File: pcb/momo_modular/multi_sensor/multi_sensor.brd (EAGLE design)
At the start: 100 x 33 mm, 38 parts, among them U1 MCP6001U, U10 SM5470-DIFF-PRESS-SENSOR, U2 16LF1847, U3 DUAL-BUFFER-OD-NC7WZ07, U4 LT1990, U5 2:1-MUX, U6 2:1-MUX, U7 AD8557-DIGITRIM-OPAMP, U8 2:1-MUX, U9 2:1-MUX

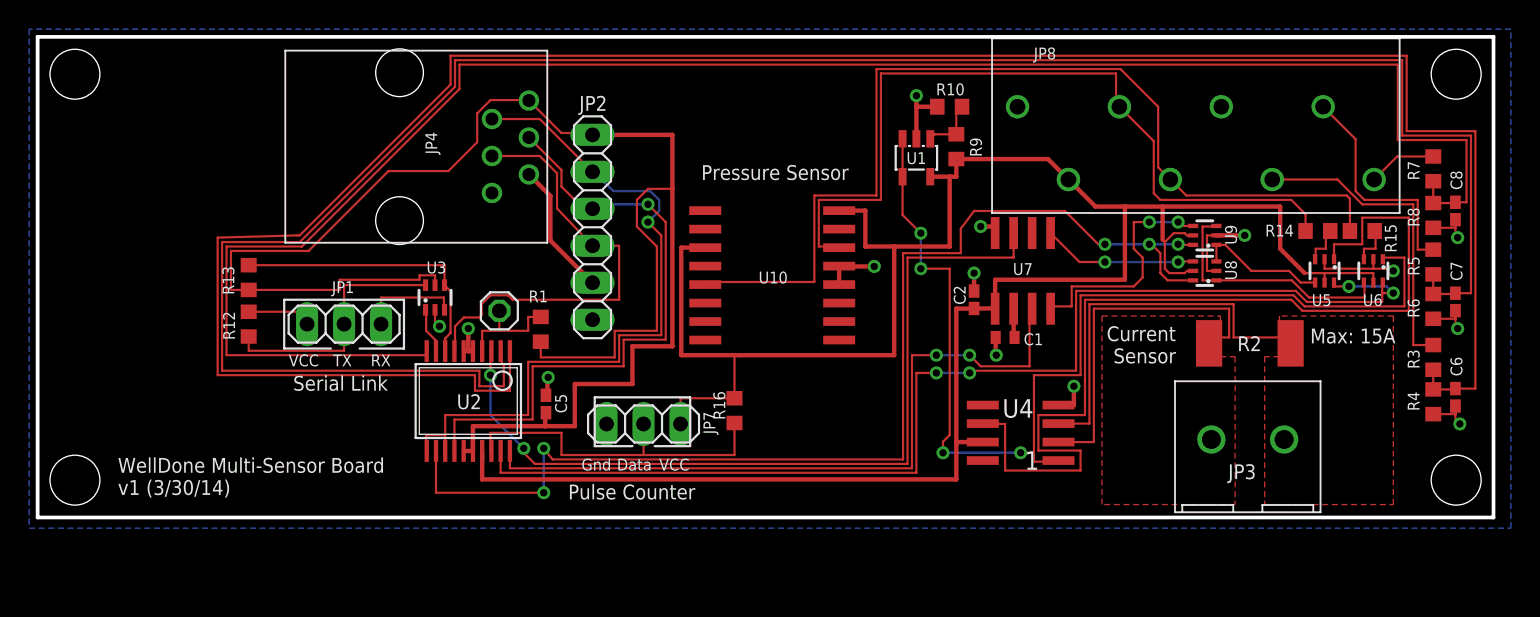
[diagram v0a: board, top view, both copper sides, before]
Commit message: Update BOM descriptions and footprints
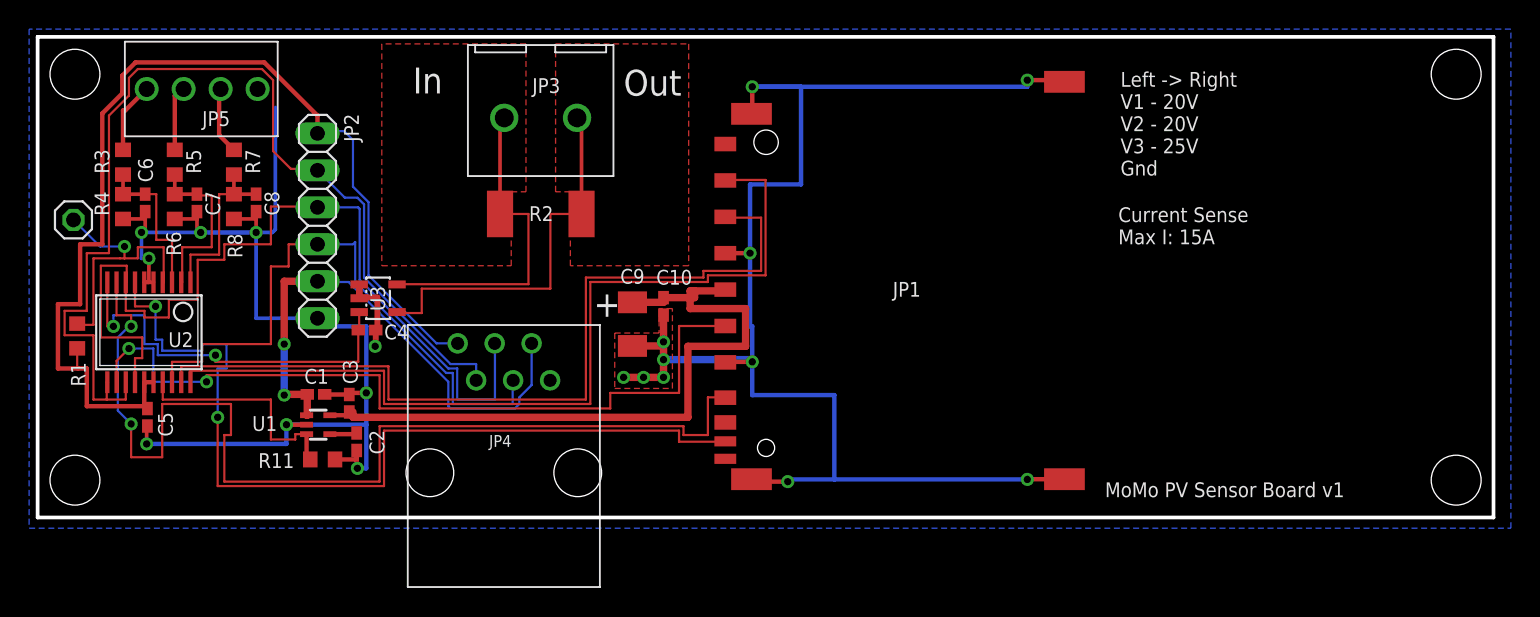
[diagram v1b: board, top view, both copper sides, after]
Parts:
- removed JP7: (no value), pinhead:1X03
- removed JP8: 8PIN-TERMBLOCK-PUSH, components:8-PIN-TERMBLOCK-PUSH
- removed R10: 357K, rcl:R0603
- removed R12, R13, R14, R15, R16: 10K, rcl:R0603
- removed R9: 649K, rcl:R0603
- removed U10: SM5470-DIFF-PRESS-SENSOR, components:SO16W
- removed U4: LT1990, components:SOP08
- removed U5, U6, U8, U9: 2:1-MUX, components:SOT363_INFINEON
- removed U7: AD8557-DIGITRIM-OPAMP, components:SOIC8
- added C10: 100 nF, rcl:C0402K
- added C3: 1 uF, rcl:C0402K
- added C4: 47 nF, rcl:C0402K
- added C9: 22 uF, rcl:C1206K
- added JP5: SCREWTERM4, components:SCREWTERM4
- added R11: 100K, rcl:R0603
- C1: value 10 nF -> 1 uF; device rcl:C0402 -> rcl:C0402K
- JP1: value (none) -> SDCARD-HOLDER; device pinhead:1X03 -> components:SDHOLDER-9PIN
- R3, R5: value 931K -> 620K 1%
- R4, R6, R8: value 66.5K -> 100K 1%
- R7: value 931K -> 806K 1%
- U1: value MCP6001U -> AP7115-LDO; device components:SOT23-5L -> components:SOT353
- U3: value DUAL-BUFFER-OD-NC7WZ07 -> TS1100; device components:SC70-6L -> components:SOT23-5L
- moved R3 91.0 mm to (9.65, 28.2)
- moved R4 91.0 mm to (9.65, 25.1)
- moved C6 91.0 mm to (11.2, 25.4)
- moved R5 86.7 mm to (13.2, 28.2)
- moved R6 86.7 mm to (13.2, 25.1)
- moved C7 86.7 mm to (14.7, 25.4)
- moved R8 82.4 mm to (17.3, 25.1)
- moved C8 82.4 mm to (18.8, 25.4)
- moved R7 82.4 mm to (17.3, 28.2)
- moved JP3 54.3 mm to (37.8, 31.2), turned to 180 degrees
- moved R2 49.5 mm to (38.4, 24.6), turned to 180 degrees
- moved C1 47.5 mm to (22.9, 12.2), turned to 0 degrees
- moved U1 45.0 mm to (23.1, 10.2), turned to 270 degrees
- moved C2 43.5 mm to (25.7, 8.99), turned to 270 degrees
- moved R1 31.9 mm to (6.50, 16.3)
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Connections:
- removed net AN-INVERT: U2.12, U8.6, U9.6
- removed net AN-SELECT: U2.19, U5.6, U6.6
- removed net AN-VOL: U2.3, U7.7
- removed net DATA_RX: JP1.3, U3.3
- removed net DATA_TX: JP1.2, R12.1, U3.6
- removed net DIFF+: JP8.6, R14.2, U10.14
- removed net DIFF-: JP8.5, R15.2, U10.5
- removed net N$13: U7.5, U8.4
- removed net N$14: U7.4, U9.4
- removed net N$16: U4.6, U5.1
- removed net N$2: JP1.1, R12.2
- removed net N$5: U5.4, U8.3, U9.1
- removed net N$6: R14.1, U5.3
- removed net N$7: C1.1, U7.2
- removed net N$8: U6.4, U8.1, U9.3
- removed net N$9: R15.1, U6.3
- removed net PROG-AMP: U2.20, U7.3
- removed net PULSE-IN: JP7.2, R16.1, U2.18
- removed net RX: R13.1, U2.8, U3.4
- removed net TX: U2.9, U3.1
- removed net V1_IN: JP8.3, R3.2
- removed net V2_IN: JP8.2, R5.2
- removed net V3_IN: JP8.1, R7.2
- removed net VANALOG: C2.1, JP7.1, JP8.7, R16.2, R9.2, U1.5, U10.16, U10.3, U2.17, U4.7, U5.5, U6.5, U7.1, U8.5, U9.5
- removed net VREF: U1.3, U1.4, U4.1, U6.1
- new net CDET: JP1.CDETECT, U2.7
- new net CS: JP1.1, U2.20
- new net ISENSE: C4.1, U2.10, U3.3
- new net N$10: JP5.P$1, R3.2
- new net N$11: JP5.P$2, R5.2
- new net N$12: JP5.P$3, R7.2
- new net REG_EN: R11.2, U1.3, U2.17
- new net SCK: JP1.5, U2.12
- new net SD0: JP1.2, U2.19
- new net SDI: JP1.7, U2.9
- new net VCCIO: C10.1, C3.1, C9.1, JP1.4, U1.5
- net ALARM: now also U2.18; no longer U2.7
- net GND: now also C10.2, C3.2, C4.2, C9.2, JP1.3, JP1.6, JP1.CDGND, JP1.CDGND_BOT, JP1.WPGND, JP1.WPGND_BOT, JP5.P$4, R11.1, U3.1; no longer JP7.3, JP8.8, R10.1, U10.12, U10.13, U4.4, U5.2, U6.2, U7.8, U8.2, U9.2
- net N$3: now also C2.1, U1.4; no longer R10.2, R9.1, U1.1
- net RS+: now also JP3.P$2, R2.2, U3.5; no longer JP3.P$1, R2.1, U4.2
- net RS-: now also JP3.P$1, R2.1, U3.4; no longer JP3.P$2, R2.2, U4.3
- net SDA: now also U2.8
- net V+: now also C1.1, U1.1
- net V1: now also U2.3; no longer U2.1
- net V3: now also U2.1; no longer U2.10
- net VCCINT: no longer R13.2, U3.5
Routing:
- net VANALOG: track 168.1 -> 0.00 mm
- net GND: track 40.1 -> 193.9 mm, vias 14 -> 20
- net V1: track 153.3 -> 10.8 mm
- net V2: track 143.9 -> 12.0 mm
- net V3: track 126.2 -> 11.9 mm
- net AN-SELECT: track 81.8 -> 0.00 mm, vias 4 -> 0
- net AN-INVERT: track 80.6 -> 0.00 mm, vias 5 -> 0
- net VREF: track 74.6 -> 0.00 mm, vias 4 -> 0
- net SDI: track 0.00 -> 71.6 mm, vias 0 -> 2
- net DIFF-: track 67.4 -> 0.00 mm
- net N$16: track 64.7 -> 0.00 mm
- net CDET: track 0.00 -> 61.3 mm, vias 0 -> 2
- net CS: track 0.00 -> 60.8 mm
- net SD0: track 0.00 -> 58.2 mm
- net AN-VOL: track 57.8 -> 0.00 mm, vias 2 -> 0
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- added copper zone on layer 1, net GND
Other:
- board text added: "+"
- board text added: "Current Sense Max I: 15A"
- board text added: "In"
- board text added: "Left -> Right V1 - 20V V2 - 20V V3 - 25V Gnd"
- board text added: "MoMo PV Sensor Board v1"
- board text added: "Out"
- board text removed: "Current Sensor"
- board text removed: "Data"
- board text removed: "Gnd"
- board text removed: "Max: 15A"
- board text removed: "Pressure Sensor"
- board text removed: "Pulse Counter"
- board text removed: "RX"
- board text removed: "Serial Link"
- board text removed: "TX"
- board text removed: "VCC"
- board text removed: "WellDone Multi-Sensor Board v1 (3/30/14)"

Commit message: Final layout touches
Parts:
- removed C10: 100 nF, rcl:C0402K
- removed C3: 1 uF, rcl:C0402K
- removed C4: 47 nF, rcl:C0402K
- removed C9: 22 uF, rcl:C1206K
- removed JP5: SCREWTERM4, components:SCREWTERM4
- removed R11: 100K, rcl:R0603
- added JP7: (no value), pinhead:1X03
- added JP8: 8PIN-TERMBLOCK-PUSH, components:8-PIN-TERMBLOCK-PUSH
- added R10: 357K, rcl:R0603
- added R12, R13, R14, R15, R16: 10K, rcl:R0603
- added R9: 649K, rcl:R0603
- added U10: SM5470-DIFF-PRESS-SENSOR, components:SO16W
- added U4: LT1990, components:SOP08
- added U5, U6, U8, U9: 2:1-MUX, components:SOT363_INFINEON
- added U7: AD8557-DIGITRIM-OPAMP, components:SOIC8
- C1: value 1 uF -> 10 nF; device rcl:C0402K -> rcl:C0402
- JP1: value SDCARD-HOLDER -> (none); device components:SDHOLDER-9PIN -> pinhead:1X03
- R3, R5: value 620K 1% -> 931K
- R4, R6, R8: value 100K 1% -> 66.5K
- R7: value 806K 1% -> 931K
- U1: value AP7115-LDO -> MCP6001U; device components:SOT353 -> components:SOT23-5L
- U3: value TS1100 -> DUAL-BUFFER-OD-NC7WZ07; device components:SOT23-5L -> components:SC70-6L
- moved R3 91.0 mm to (99.7, 14.8)
- moved R4 91.0 mm to (99.7, 11.7)
- moved C6 91.0 mm to (101.2, 12.0)
- moved R5 86.7 mm to (99.7, 21.3)
- moved R6 86.7 mm to (99.7, 18.3)
- moved C7 86.7 mm to (101.2, 18.6)
- moved R8 82.4 mm to (99.7, 24.5)
- moved C8 82.4 mm to (101.2, 24.8)
- moved R7 82.4 mm to (99.7, 27.7)
- moved JP3 54.3 mm to (87.4, 9.14), turned to 0 degrees
- moved R2 49.5 mm to (87.1, 15.7), turned to 0 degrees
- moved C1 47.5 mm to (70.3, 16.2), turned to 180 degrees
- moved U1 45.0 mm to (64.2, 28.5), turned to 180 degrees
- moved C2 43.5 mm to (68.1, 18.7), turned to 90 degrees
- moved R1 31.9 mm to (38.4, 16.7)
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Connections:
- removed net CDET: JP1.CDETECT, U2.7
- removed net CS: JP1.1, U2.20
- removed net ISENSE: C4.1, U2.10, U3.3
- removed net N$10: JP5.P$1, R3.2
- removed net N$11: JP5.P$2, R5.2
- removed net N$12: JP5.P$3, R7.2
- removed net REG_EN: R11.2, U1.3, U2.17
- removed net SCK: JP1.5, U2.12
- removed net SD0: JP1.2, U2.19
- removed net SDI: JP1.7, U2.9
- removed net VCCIO: C10.1, C3.1, C9.1, JP1.4, U1.5
- new net AN-INVERT: U2.12, U8.6, U9.6
- new net AN-SELECT: U2.19, U5.6, U6.6
- new net AN-VOL: U2.3, U7.7
- new net DATA_RX: JP1.3, U3.3
- new net DATA_TX: JP1.2, R12.1, U3.6
- new net DIFF+: JP8.6, R14.2, U10.14
- new net DIFF-: JP8.5, R15.2, U10.5
- new net N$13: U7.5, U8.4
- new net N$14: U7.4, U9.4
- new net N$16: U4.6, U5.1
- new net N$2: JP1.1, R12.2
- new net N$5: U5.4, U8.3, U9.1
- new net N$6: R14.1, U5.3
- new net N$7: C1.1, U7.2
- new net N$8: U6.4, U8.1, U9.3
- new net N$9: R15.1, U6.3
- new net PROG-AMP: U2.20, U7.3
- new net PULSE-IN: JP7.2, R16.1, U2.18
- new net RX: R13.1, U2.8, U3.4
- new net TX: U2.9, U3.1
- new net V1_IN: JP8.3, R3.2
- new net V2_IN: JP8.2, R5.2
- new net V3_IN: JP8.1, R7.2
- new net VANALOG: C2.1, JP7.1, JP8.7, R16.2, R9.2, U1.5, U10.16, U10.3, U2.17, U4.7, U5.5, U6.5, U7.1, U8.5, U9.5
- new net VREF: U1.3, U1.4, U4.1, U6.1
- net ALARM: now also U2.7; no longer U2.18
- net GND: now also JP7.3, JP8.8, R10.1, U10.12, U10.13, U4.4, U5.2, U6.2, U7.8, U8.2, U9.2; no longer C10.2, C3.2, C4.2, C9.2, JP1.3, JP1.6, JP1.CDGND, JP1.CDGND_BOT, JP1.WPGND, JP1.WPGND_BOT, JP5.P$4, R11.1, U3.1
- net N$3: now also R10.2, R9.1, U1.1; no longer C2.1, U1.4
- net RS+: now also JP3.P$1, R2.1, U4.2; no longer JP3.P$2, R2.2, U3.5
- net RS-: now also JP3.P$2, R2.2, U4.3; no longer JP3.P$1, R2.1, U3.4
- net SDA: no longer U2.8
- net V+: no longer C1.1, U1.1
- net V1: now also U2.1; no longer U2.3
- net V3: now also U2.10; no longer U2.1
- net VCCINT: now also R13.2, U3.5
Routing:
- net VANALOG: track 0.00 -> 168.1 mm
- net GND: track 193.9 -> 40.1 mm, vias 20 -> 14
- net V1: track 10.8 -> 153.3 mm
- net V2: track 12.0 -> 143.9 mm
- net V3: track 11.9 -> 126.2 mm
- net AN-SELECT: track 0.00 -> 81.8 mm, vias 0 -> 4
- net AN-INVERT: track 0.00 -> 80.6 mm, vias 0 -> 5
- net VREF: track 0.00 -> 74.6 mm, vias 0 -> 4
- net SDI: track 71.6 -> 0.00 mm, vias 2 -> 0
- net DIFF-: track 0.00 -> 67.4 mm
- net N$16: track 0.00 -> 64.7 mm
- net CDET: track 61.3 -> 0.00 mm, vias 2 -> 0
- net CS: track 60.8 -> 0.00 mm
- net SD0: track 58.2 -> 0.00 mm
- net AN-VOL: track 0.00 -> 57.8 mm, vias 0 -> 2
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- removed copper zone on layer 1, net GND
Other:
- board text added: "Current Sensor"
- board text added: "Data"
- board text added: "Gnd"
- board text added: "Max: 15A"
- board text added: "Pressure Sensor"
- board text added: "Pulse Counter"
- board text added: "RX"
- board text added: "Serial Link"
- board text added: "TX"
- board text added: "VCC"
- board text added: "WellDone Multi-Sensor Board v1 (3/30/14)"
- board text removed: "+"
- board text removed: "Current Sense Max I: 15A"
- board text removed: "In"
- board text removed: "Left -> Right V1 - 20V V2 - 20V V3 - 25V Gnd"
- board text removed: "MoMo PV Sensor Board v1"
- board text removed: "Out"

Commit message: Connect Vclamp and Vdd on in-amp
Vclamp is specified to not be floating even when not in use.
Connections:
- net VANALOG: now also U7.6
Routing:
- net VANALOG: track 168.1 -> 171.3 mm
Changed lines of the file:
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@@
 <wire x1="69.5706" y1="18.1452" x2="68.1228" y2="18.1452" width="0.3048" layer="1"/>
 <wire x1="69.5706" y1="18.1264" x2="69.5706" y2="20.1168" width="0.3048" layer="1"/>
-<wire x1="69.5706" y1="20.1168" x2="78.486" y2="20.1168" width="0.3048" layer="1"/>
+<wire x1="69.5706" y1="20.1168" x2="72.0852" y2="20.1168" width="0.3048" layer="1"/>
+<wire x1="72.0852" y1="20.1168" x2="78.486" y2="20.1168" width="0.3048" layer="1"/>
 <wire x1="78.486" y1="20.1168" x2="78.486" y2="25.146" width="0.3048" layer="1"/>
 <wire x1="68.7232" y1="8.9662" x2="66.9036" y2="8.9662" width="0.3048" layer="1"/>
@@
 <wire x1="47.9552" y1="10.2108" x2="47.9552" y2="11.9752" width="0.1524" layer="1"/>
 <wire x1="47.9552" y1="11.9752" x2="51.6636" y2="11.9752" width="0.1524" layer="1"/>
+<contactref element="U7" pad="6"/>
+<wire x1="72.1106" y1="23.3264" x2="72.0852" y2="23.3264" width="0.1524" layer="1"/>
+<wire x1="72.0852" y1="23.3264" x2="72.0852" y2="20.1168" width="0.1524" layer="1"/>
 </signal>
 <signal name="VREF">

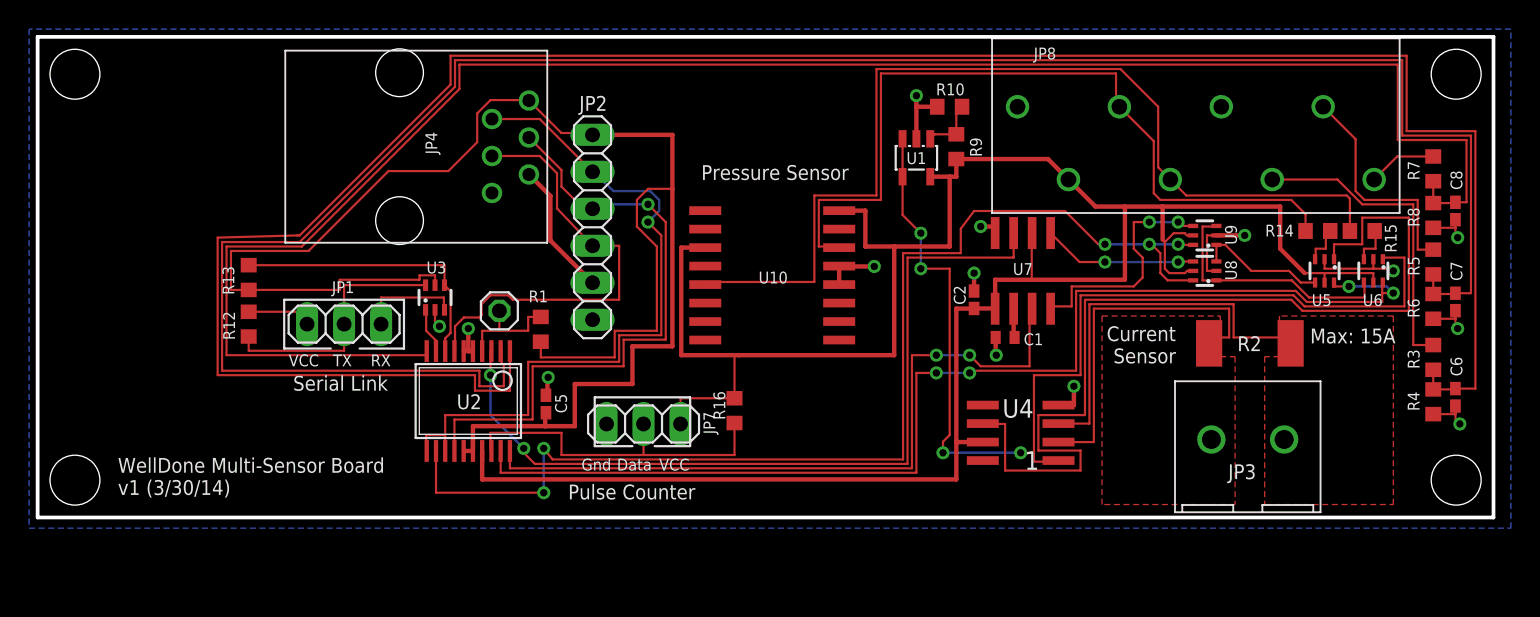
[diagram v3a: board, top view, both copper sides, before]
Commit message: Fix multisensor board layout
- Add separate power supply for analog circuitry to
maintain voltage requirement.
- Fix data line connection on MIB bus
- Remove incorrect pin headers
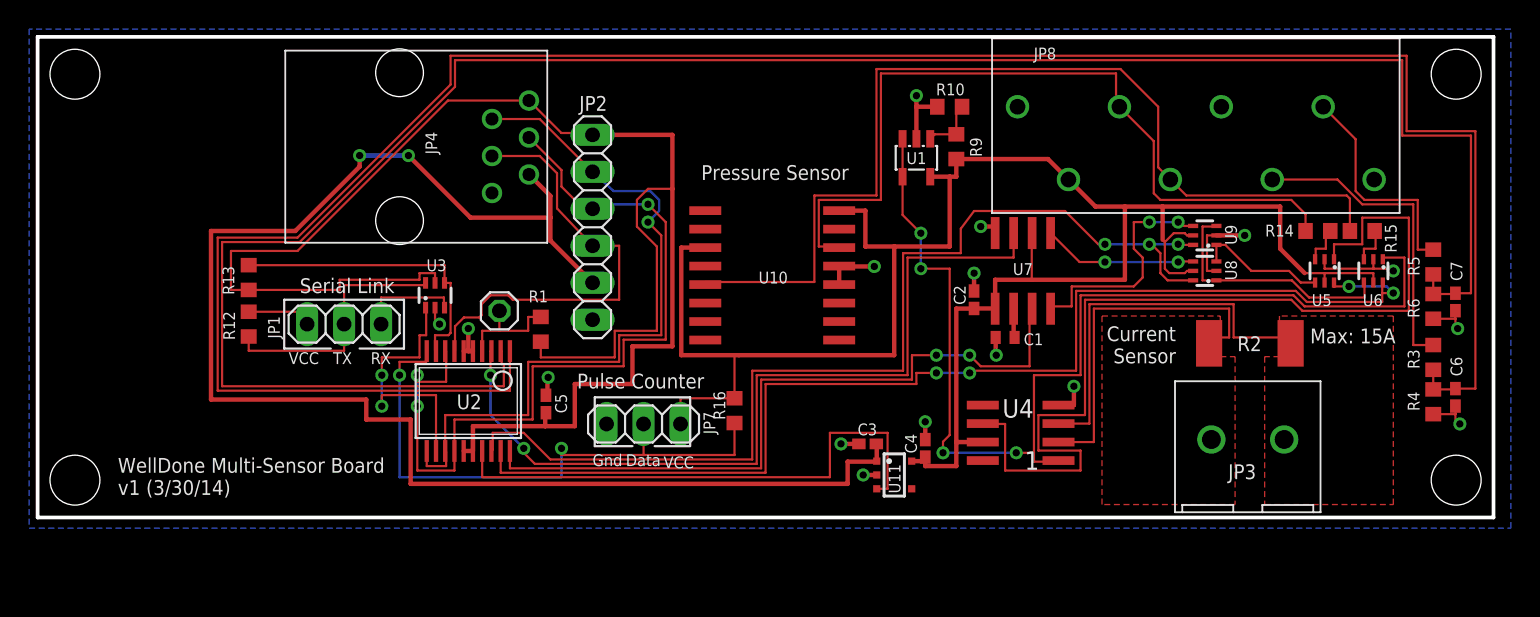
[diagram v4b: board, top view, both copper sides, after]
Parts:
- removed C8: 100 nF, rcl:C0402K
- removed R7: 931K, rcl:R0603
- removed R8: 66.5K, rcl:R0603
- added C3: 100 nF, rcl:C0402K
- added C4: 1 uF, rcl:C0402K
- added U11: TCR2EF28-LINREG, components:SC74A-5PIN
- moved U3 0.15 mm to (31.1, 19.1)
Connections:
- removed net V3: C8.1, R7.1, R8.2, U2.10
- new net AN-ENABLE: U11.3, U2.17
- net AN-INVERT: now also U2.18; no longer U2.12
- net GND: now also C3.2, C4.2, U11.2; no longer C8.2, R8.1
- net PULSE-IN: now also U2.10; no longer U2.18
- net RX: now also U2.9; no longer U2.8
- net SDA: now also U2.8
- net TX: now also U2.12; no longer U2.9
- net V+: now also C3.1, U11.1
- net V3_IN: no longer R7.2
- net VANALOG: now also C4.1, U11.5; no longer U2.17
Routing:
- net V3: track 126.2 -> 0.00 mm
- net V+: track 9.25 -> 102.8 mm, vias 0 -> 2
- net AN-ENABLE: track 0.00 -> 37.3 mm
- net VANALOG: track 171.3 -> 139.8 mm
- net PULSE-IN: track 23.9 -> 40.3 mm, vias 0 -> 2
- net TX: track 3.13 -> 18.4 mm, vias 0 -> 2
- net SDA: track 43.1 -> 58.2 mm, vias 1 -> 3
- net AN-INVERT: track 80.6 -> 72.4 mm, vias 5 -> 3
- net V3_IN: track 4.72 -> 0.00 mm
- net RX: track 19.7 -> 20.8 mm
- net VCCINT: track 115.4 -> 114.4 mm
- net SCL: track 49.4 -> 50.0 mm
- net GND: track 40.1 -> 40.7 mm, vias 14 -> 16
